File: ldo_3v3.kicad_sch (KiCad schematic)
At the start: 4 parts, among them U405 SE8633K2-HF

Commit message: Finish the board redesign with SoM on the bottom
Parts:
- renumbered C402 to C3701, C406 to C3702, TP402 to TP3701, U405 to U3701
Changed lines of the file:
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@@
 		(on_board yes)
 		(dnp no)
-		(property "Reference" "TP402"
+		(property "Reference" "TP3701"
 			(at 160.02 94.4881 0)
 			(effects
@@
 			(project "HALPI2"
 				(path "/abc482bd-3f17-4d35-80db-1da3dcdb5c27/c7bf4e1f-6bd1-4be7-9e56-1bd438bf5d42/949897e8-9bb6-4c13-b9c6-3f831f2e4c69/0d843d07-83df-4f55-a68d-3751ed9e506d"
-					(reference "TP402")
+					(reference "TP3701")
 					(unit 1)
 				)
@@
 		(on_board yes)
 		(dnp no)
-		(property "Reference" "C406"
+		(property "Reference" "C3702"
 			(at 169.291 101.7016 0)
 			(effects
@@
 			)
 		)
-		(property "Description" ""
+		(property "Description" "Unpolarized capacitor"
 			(at 166.37 102.87 0)
 			(effects
@@
 			(project "HALPI2"
 				(path "/abc482bd-3f17-4d35-80db-1da3dcdb5c27/c7bf4e1f-6bd1-4be7-9e56-1bd438bf5d42/949897e8-9bb6-4c13-b9c6-3f831f2e4c69/0d843d07-83df-4f55-a68d-3751ed9e506d"
-					(reference "C406")
+					(reference "C3702")
 					(unit 1)
 				)
@@
 		(dnp no)
 		(fields_autoplaced yes)
-		(property "Reference" "U405"
+		(property "Reference" "U3701"
 			(at 146.05 90.17 0)
 			(effects
@@
 			)
 		)
-		(property "Description" "200mA 85dB Fixed 3.3V Positive electrode 80V SOT-89-3 Voltage Regulators - Linear, Low Drop Out (LDO) Regulators ROHS"
+		(property "Description" "Generic 3-terminal voltage regulator, Alternate KiCad Library"
 			(at 146.05 99.06 0)
 			(effects
@@
 			(project "HALPI2"
 				(path "/abc482bd-3f17-4d35-80db-1da3dcdb5c27/c7bf4e1f-6bd1-4be7-9e56-1bd438bf5d42/949897e8-9bb6-4c13-b9c6-3f831f2e4c69/0d843d07-83df-4f55-a68d-3751ed9e506d"
-					(reference "U405")
+					(reference "U3701")
 					(unit 1)
 				)
@@
 		(on_board yes)
 		(dnp no)
-		(property "Reference" "C402"
+		(property "Reference" "C3701"
 			(at 124.079 101.7016 0)
 			(effects
@@
 			)
 		)
-		(property "Description" ""
+		(property "Description" "Unpolarized capacitor"
 			(at 127 102.87 0)
 			(effects
@@
 			(project "HALPI2"
 				(path "/abc482bd-3f17-4d35-80db-1da3dcdb5c27/c7bf4e1f-6bd1-4be7-9e56-1bd438bf5d42/949897e8-9bb6-4c13-b9c6-3f831f2e4c69/0d843d07-83df-4f55-a68d-3751ed9e506d"
-					(reference "C402")
-					(unit 1)
-				)
+					(reference "C3701")
+					(unit 1)
+				)

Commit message: Further refinements
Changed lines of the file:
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@@
+			)
+		)
+		(property "LCSC Part" ""
+			(at 157.48 96.52 0)
+			(effects
+				(font
+					(size 1.27 1.27)
+				)
+			)
+		)
+		(property "Sim.Enable" ""
+			(at 157.48 96.52 0)
+			(effects
+				(font
+					(size 1.27 1.27)
+				)
 			)
 		)
@@
 			)
 		)
+		(property "LCSC Part" ""
+			(at 166.37 102.87 0)
+			(effects
+				(font
+					(size 1.27 1.27)
+				)
+			)
+		)
+		(property "Sim.Enable" ""
+			(at 166.37 102.87 0)
+			(effects
+				(font
+					(size 1.27 1.27)
+				)
+			)
+		)
 		(pin "1"
 		)
@@
 					(size 1.27 1.27)
 				)
+				(hide yes)
+			)
+		)
+		(property "Sim.Enable" ""
+			(at 146.05 96.52 0)
+			(effects
+				(font
+					(size 1.27 1.27)
+				)
 			)
 		)
@@
 			)
 		)
+		(property "LCSC Part" ""
+			(at 127 102.87 0)
+			(effects
+				(font
+					(size 1.27 1.27)
+				)
+			)
+		)
+		(property "Sim.Enable" ""
+			(at 127 102.87 0)
+			(effects
+				(font
+					(size 1.27 1.27)
+				)
+			)
+		)

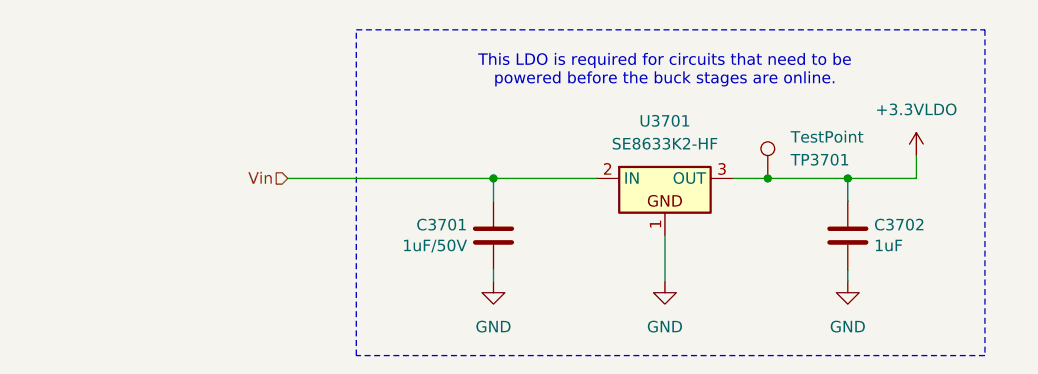
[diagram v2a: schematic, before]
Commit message: Change MCU to RP2040
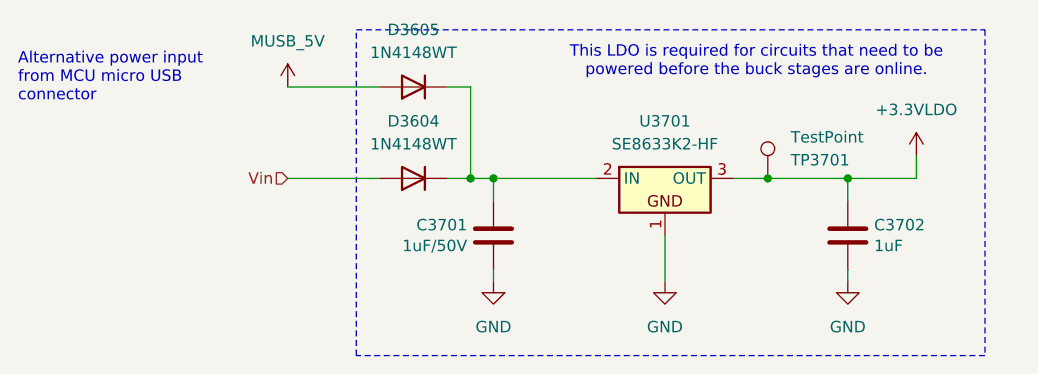
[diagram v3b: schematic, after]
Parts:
- added D3604, D3605: 1N4148WT, Diode_SMD:D_SOD-523, symbol Device:D
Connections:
- net Vin: now also D3604.2 (A); no longer C3701.1, U3701.2 (IN)
- new net: C3701.1, D3604.1 (K), D3605.1 (K), U3701.2 (IN)
- new net MUSB_5V: D3605.2 (A)
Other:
- note added: "Alternative power input from MCU micro USB connector"
